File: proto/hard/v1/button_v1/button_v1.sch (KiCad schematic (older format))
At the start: 61 parts, among them J1 Conn_01x06_Female, J10 Conn_01x04_Male, J14 K3-2235D, J2 Conn_01x06_Female, J3 Conn_01x06_Female, J4 Conn_01x06_Female, J7 Conn_01x04_Female, J9 Conn_01x06_Male, Q1 TP0610T, Q3 TP0610T, Q6 UMG8N, Q7 UMG8N, Q8 IRLML2803, U1 LCD_2.8_SPI, U11 TC305, U12 LCD_1_8_SPI, U13 74HC595, U2 STM32F103C8Tx, U6 LM339, Y1 8MHz

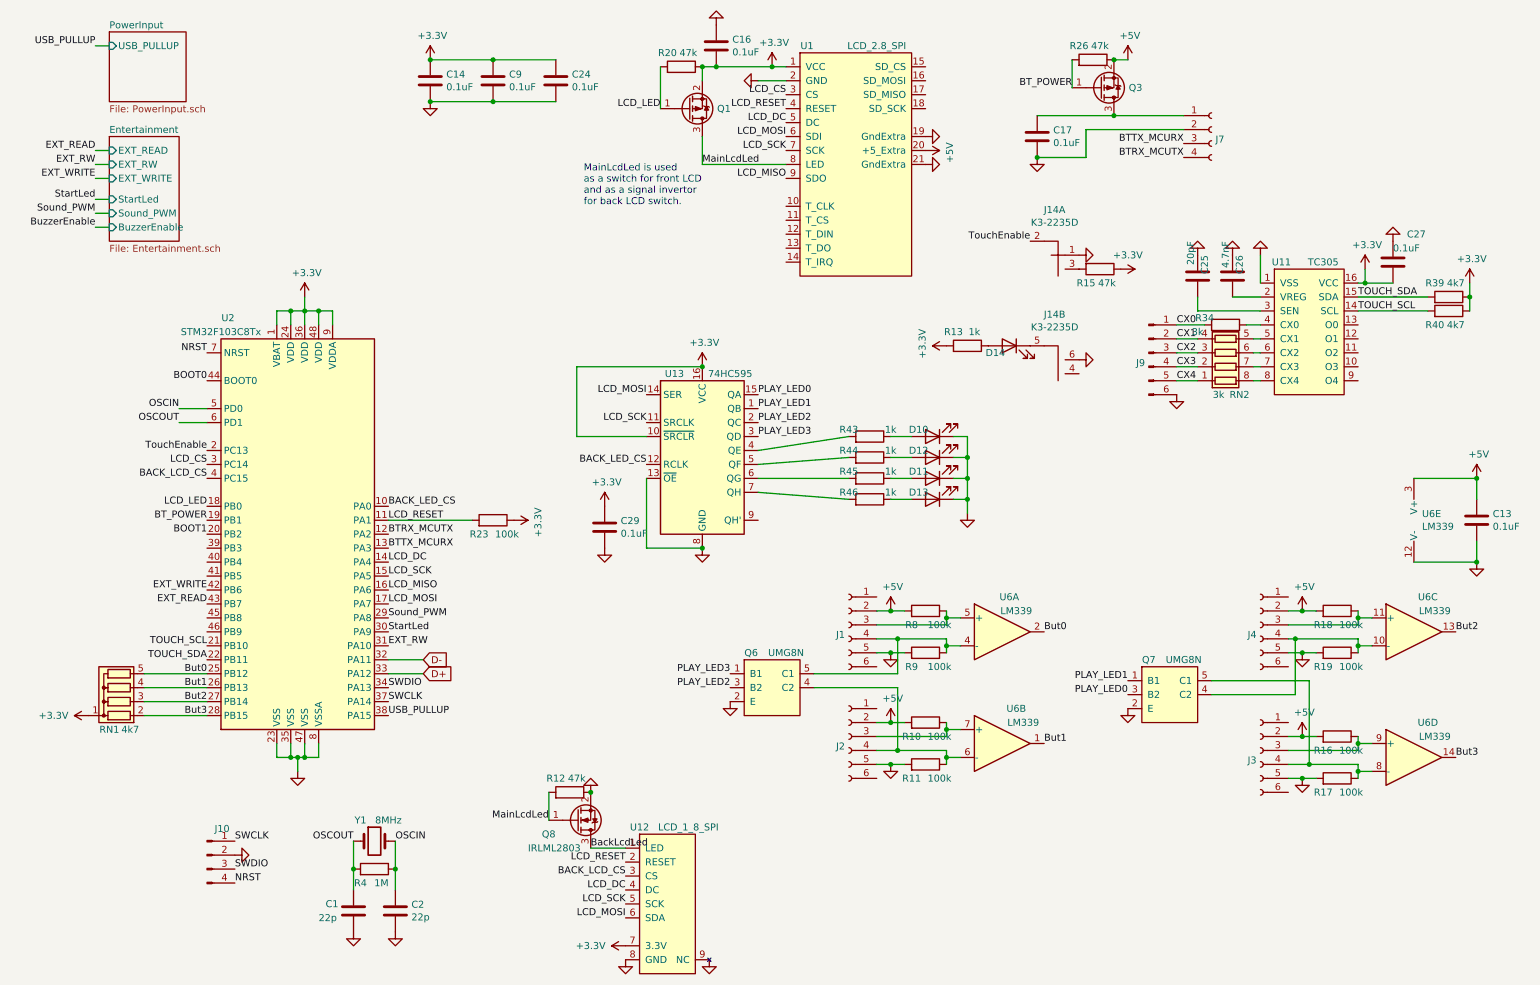
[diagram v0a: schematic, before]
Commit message: Moved buttons to separate sheet. Added replacement transistors for buttons.
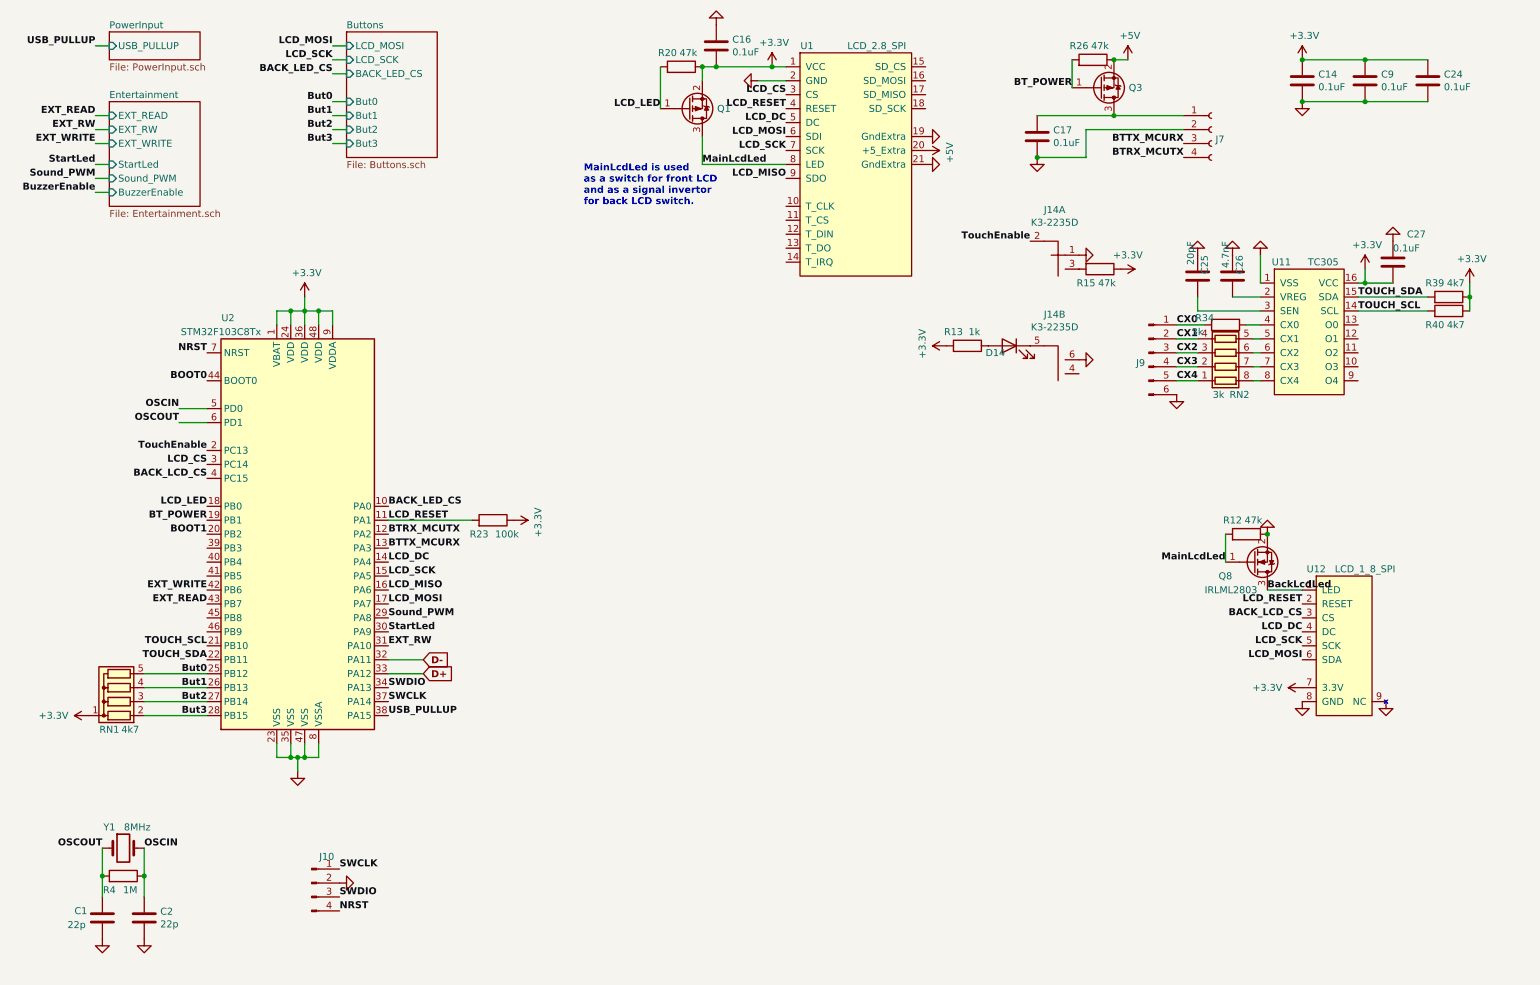
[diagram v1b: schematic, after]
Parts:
- removed C13, C29: 0.1uF, Capacitor_SMD:C_0805_2012Metric_Pad1.15x1.40mm_HandSolder, symbol Device:C
- removed D10, D11, D12, D13: LED, LED_THT:LED_D3.0mm_Clear, symbol Device:LED
- removed J1, J2, J3, J4: Conn_01x06_Female, Connector_RJ:RJ12_Amphenol_54601, symbol Connector:Conn_01x06_Female
- removed Q6, Q7: UMG8N, Package_TO_SOT_SMD:SOT-353_SC-70-5_Handsoldering, symbol brbuttonsystem:UMG8N
- removed R10, R11, R16, R17, R18, R19, R8, R9: 100k, Resistor_SMD:R_0805_2012Metric_Pad1.15x1.40mm_HandSolder, symbol Device:R
- removed R43, R44, R45, R46: 1k, Resistor_SMD:R_0805_2012Metric_Pad1.15x1.40mm_HandSolder, symbol Device:R
- removed U13: 74HC595, Package_SO:SOIC-16_3.9x9.9mm_P1.27mm, symbol 74xx:74HC595
- removed U6: LM339, Package_SO:SOIC-14_3.9x8.7mm_P1.27mm, symbol Comparator:LM339
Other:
- moved on the sheet: C1, C14, C2, C24, C9, J10, Q8, R12, R4, U12, Y1

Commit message: BOOT0 connected to GND Due to migration to Kicad V5.1.6 had to change text style from "bold" to "normal"
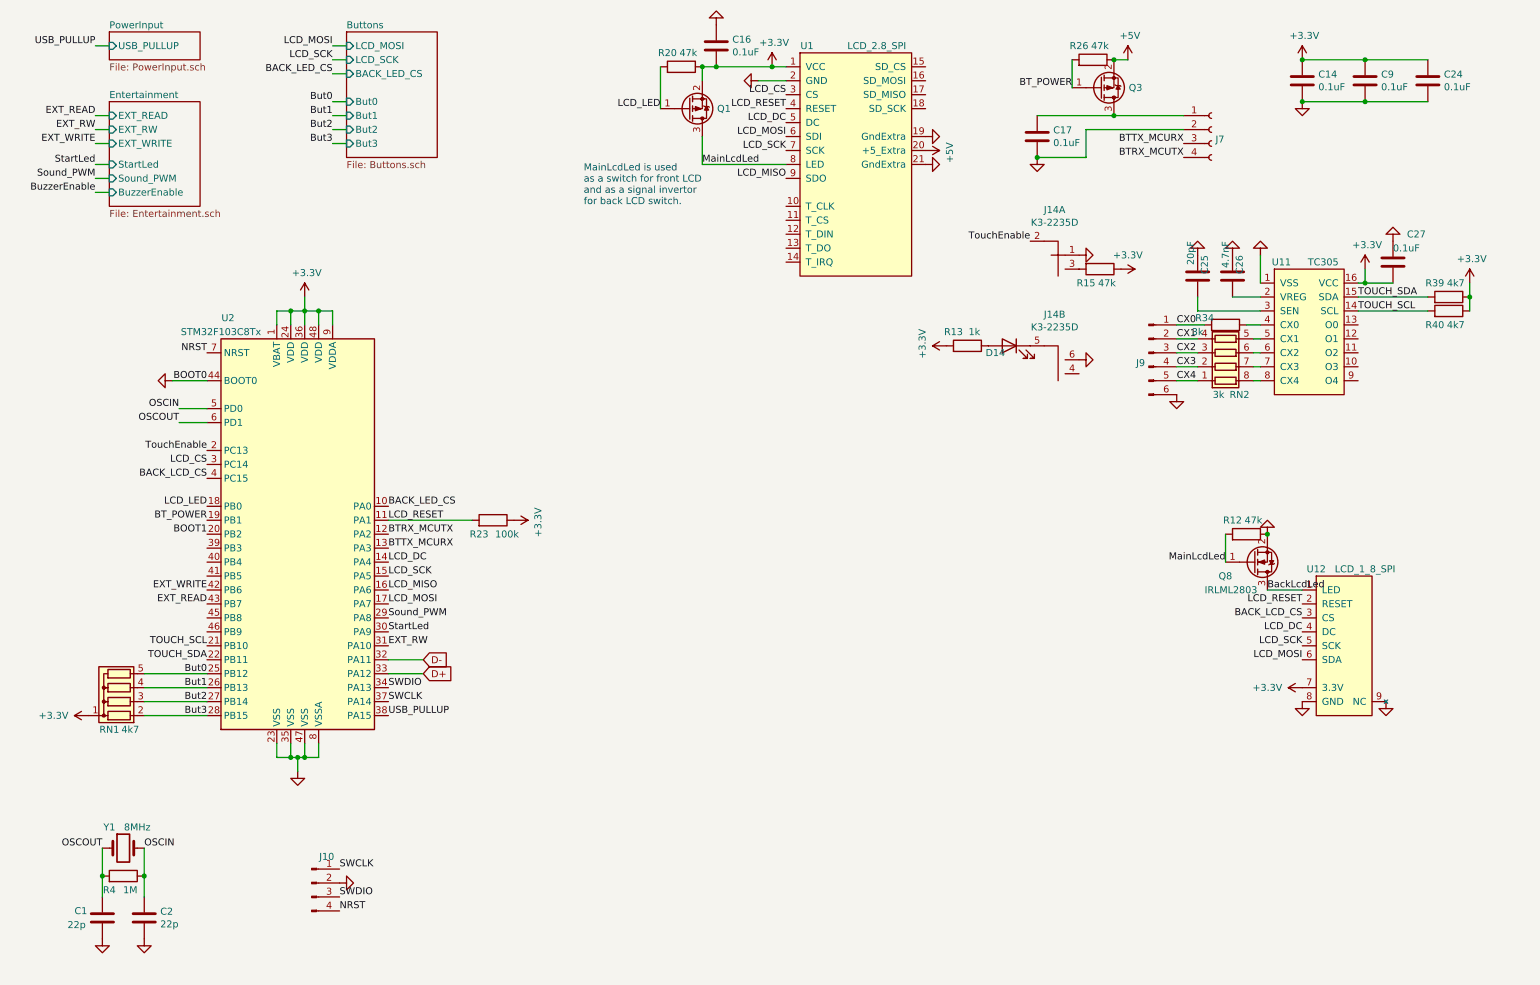
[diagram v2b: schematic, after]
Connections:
- net BOOT0 is gone; now on net GND: U2.44 (BOOT0)
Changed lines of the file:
@@
 EESchema Schematic File Version 4
-LIBS:button_v1-cache
-EELAYER 29 0
+EELAYER 30 0
 EELAYER END
 $Descr A4 11693 8268
@@
 	1    0    0    -1
 $EndComp
-Text Label 1400 6550 0    50   ~ 6
+Text Label 1400 6550 0    50   ~ 0
 OSCIN
-Text Label 1100 6550 2    50   ~ 6
+Text Label 1100 6550 2    50   ~ 0
 OSCOUT
 $Comp
@@
 Wire Wire Line
 	6000 950  5900 950
-Text Label 6000 1450 2    50   ~ 6
+Text Label 6000 1450 2    50   ~ 0
 LCD_MOSI
-Text Label 6000 1750 2    50   ~ 6
+Text Label 6000 1750 2    50   ~ 0
 LCD_MISO
-Text Label 6000 1550 2    50   ~ 6
+Text Label 6000 1550 2    50   ~ 0
 LCD_SCK
 $Comp
@@
 Wire Wire Line
 	5400 1650 6000 1650
-Text Label 5100 1250 2    50   ~ 6
+Text Label 5100 1250 2    50   ~ 0
 LCD_LED
-Text Label 6000 1250 2    50   ~ 6
+Text Label 6000 1250 2    50   ~ 0
 LCD_RESET
-Text Label 6000 1150 2    50   ~ 6
+Text Label 6000 1150 2    50   ~ 0
 LCD_CS
-Text Label 6000 1350 2    50   ~ 6
+Text Label 6000 1350 2    50   ~ 0
 LCD_DC
 $Comp
@@
 Wire Wire Line
 	3750 4200 3150 4200
-Text Label 1850 5100 2    50   ~ 6
+Text Label 1850 5100 2    50   ~ 0
 TOUCH_SCL
-Text Label 1850 5200 2    50   ~ 6
+Text Label 1850 5200 2    50   ~ 0
 TOUCH_SDA
-Text Label 3150 4900 0    50   ~ 6
+Text Label 3150 4900 0    50   ~ 0
 Sound_PWM
-Text Label 1850 4200 2    50   ~ 6
+Text Label 1850 4200 2    50   ~ 0
 BT_POWER
-Text Label 3150 4400 0    50   ~ 6
+Text Label 3150 4400 0    50   ~ 0
 BTTX_MCURX
-Text Label 3150 4300 0    50   ~ 6
+Text Label 3150 4300 0    50   ~ 0
 BTRX_MCUTX
-Text Label 3150 5000 0    50   ~ 6
+Text Label 3150 5000 0    50   ~ 0
 StartLed
-Text Label 3150 5100 0    50   ~ 6
+Text Label 3150 5100 0    50   ~ 0
 EXT_RW
-Text Label 1850 4800 2    50   ~ 6
+Text Label 1850 4800 2    50   ~ 0
 EXT_READ
-Text Label 1850 4700 2    50   ~ 6
+Text Label 1850 4700 2    50   ~ 0
 EXT_WRITE
 $Comp
@@
 	0    1    -1   0
 $EndComp
-Text Label 1850 3800 2    50   ~ 6
+Text Label 1850 3800 2    50   ~ 0
 LCD_CS
-Text Label 3150 4200 0    50   ~ 6
+Text Label 3150 4200 0    50   ~ 0
 LCD_RESET
-Text Label 3150 4500 0    50   ~ 6
+Text Label 3150 4500 0    50   ~ 0
 LCD_DC
-Text Label 1850 4100 2    50   ~ 6
+Text Label 1850 4100 2    50   ~ 0
 LCD_LED
-Text Label 3150 4600 0    50   ~ 6
+Text Label 3150 4600 0    50   ~ 0
 LCD_SCK
-Text Label 3150 4700 0    50   ~ 6
+Text Label 3150 4700 0    50   ~ 0
 LCD_MISO
 $Comp
@@
 	1    0    0    -1
 $EndComp
-Text Label 3150 4800 0    50   ~ 6
+Text Label 3150 4800 0    50   ~ 0
 LCD_MOSI
 $Comp
@@
 	0    -1   -1   0
 $EndComp
-Text Label 1850 5600 2    50   ~ 6
+Text Label 1850 5600 2    50   ~ 0
 But3
-Text Label 1850 5500 2    50   ~ 6
+Text Label 1850 5500 2    50   ~ 0
 But2
-Text Label 1850 5400 2    50   ~ 6
+Text Label 1850 5400 2    50   ~ 0
 But1
-Text Label 1850 5300 2    50   ~ 6
+Text Label 1850 5300 2    50   ~ 0
 But0
 Wire Wire Line
@@
 Wire Wire Line
 	1650 3400 1850 3400
-Text Label 1650 3400 2    50   ~ 6
+Text Label 1650 3400 2    50   ~ 0
 OSCIN
-Text Label 1650 3500 2    50   ~ 6
+Text Label 1650 3500 2    50   ~ 0
 OSCOUT
 Wire Wire Line
@@
 	1    0    0    -1
 $EndComp
-Text Label 3150 5400 0    50   ~ 6
+Text Label 3150 5400 0    50   ~ 0
 SWDIO
-Text Label 3150 5500 0    50   ~ 6
+Text Label 3150 5500 0    50   ~ 0
 SWCLK
-Text Label 1850 3000 2    50   ~ 6
-NRST
-Text Label 1850 3200 2    50   ~ 6
+Text Label 1850 3200 2    50   ~ 0
 BOOT0
-Text Label 1850 4300 2    50   ~ 6
+Text Label 1850 4300 2    50   ~ 0
 BOOT1
-Text Label 1850 3700 2    50   ~ 6
+Text Label 1850 3700 2    50   ~ 0
 TouchEnable
 $Comp
@@
 Wire Wire Line
 	8050 900  8050 1100
-Text Label 8050 1100 2    50   ~ 6
+Text Label 8050 1100 2    50   ~ 0
 BT_POWER
 $Comp
@@
 	0    -1   -1   0
 $EndComp
-Text Label 7750 2200 2    50   ~ 6
+Text Label 7750 2200 2    50   ~ 0
 TouchEnable
 $Comp
@@
 	0    -1   -1   0
 $EndComp
-Text Label 8800 3200 0    50   ~ 6
+Text Label 8800 3200 0    50   ~ 0
 CX4
-Text Label 8800 3100 0    50   ~ 6
+Text Label 8800 3100 0    50   ~ 0
 CX3
-Text Label 8800 3000 0    50   ~ 6
+Text Label 8800 3000 0    50   ~ 0
 CX2
-Text Label 8800 2900 0    50   ~ 6
+Text Label 8800 2900 0    50   ~ 0
 CX1
-Text Label 8800 2800 0    50   ~ 6
+Text Label 8800 2800 0    50   ~ 0
 CX0
 Wire Wire Line
@@
 	0    1    -1   0
 $EndComp
-Text Label 10100 2600 0    50   ~ 6
+Text Label 10100 2600 0    50   ~ 0
 TOUCH_SDA
 Wire Wire Line
 	10150 2500 10350 2500
-Text Label 10100 2700 0    50   ~ 6
+Text Label 10100 2700 0    50   ~ 0
 TOUCH_SCL
 Connection ~ 10150 2500
@@
 F7 "BuzzerEnable" I L 1150 1850 50
 $EndSheet
-Text Label 1050 1300 2    50   ~ 6
+Text Label 1050 1300 2    50   ~ 0
 EXT_READ
-Text Label 1050 1400 2    50   ~ 6
+Text Label 1050 1400 2    50   ~ 0
 EXT_RW
-Text Label 1050 1500 2    50   ~ 6
+Text Label 1050 1500 2    50   ~ 0
 EXT_WRITE
-Text Label 1050 1650 2    50   ~ 6
+Text Label 1050 1650 2    50   ~ 0
 StartLed
-Text Label 1050 1750 2    50   ~ 6
+Text Label 1050 1750 2    50   ~ 0
 Sound_PWM
 Wire Wire Line
@@
 Wire Wire Line
 	1150 1300 1050 1300
-Text GLabel 3400 5300 2    50   Input ~ 6
+Text GLabel 3400 5300 2    50   Input ~ 0
 D+
-Text GLabel 3400 5200 2    50   Input ~ 6
+Text GLabel 3400 5200 2    50   Input ~ 0
 D-
 $Sheet
@@
 Connection ~ 9700 900
 Connection ~ 9700 1200
-Text Label 3150 4100 0    50   ~ 6
+Text Label 3150 4100 0    50   ~ 0
 BACK_LED_CS
-Text Label 1050 1850 2    50   ~ 6
+Text Label 1050 1850 2    50   ~ 0
 BuzzerEnable
 Wire Wire Line
 	1050 1850 1150 1850
-Text Label 2800 7000 0    50   ~ 6
+Text Label 2800 7000 0    50   ~ 0
 NRST
-Text Label 2800 6700 0    50   ~ 6
+Text Label 2800 6700 0    50   ~ 0
 SWCLK
-Text Label 2800 6900 0    50   ~ 6
+Text Label 2800 6900 0    50   ~ 0
 SWDIO
 $Comp
@@
 	1    0    0    -1
 $EndComp
-Text Label 9700 5100 2    50   ~ 6
+Text Label 9700 5100 2    50   ~ 0
 LCD_SCK
-Text Label 9700 5200 2    50   ~ 6
+Text Label 9700 5200 2    50   ~ 0
 LCD_MOSI
-Text Label 9700 5000 2    50   ~ 6
+Text Label 9700 5000 2    50   ~ 0
 LCD_DC
 $Comp
@@
 $EndComp
 Connection ~ 9450 4300
-Text Label 5400 1650 0    50   ~ 6
+Text Label 5400 1650 0    50   ~ 0
 MainLcdLed
-Text Label 9450 4700 0    50   ~ 6
+Text Label 9450 4700 0    50   ~ 0
 BackLcdLed
-Text Label 8850 1600 2    50   ~ 6
+Text Label 8850 1600 2    50   ~ 0
 BTRX_MCUTX
-Text Label 8850 1500 2    50   ~ 6
+Text Label 8850 1500 2    50   ~ 0
 BTTX_MCURX
 $Comp
@@
 	0    -1   -1   0
 $EndComp
-Text Label 9700 4900 2    50   ~ 6
+Text Label 9700 4900 2    50   ~ 0
 BACK_LCD_CS
 $Comp
@@
 	1    0    0    -1
 $EndComp
-Text Label 9700 4800 2    50   ~ 6
+Text Label 9700 4800 2    50   ~ 0
 LCD_RESET
 $Comp
@@
 	1    0    0    -1
 $EndComp
-Text Label 1850 3900 2    50   ~ 6
+Text Label 1850 3900 2    50   ~ 0
 BACK_LCD_CS
-Text Label 9150 4500 2    50   ~ 6
-MainLcdLed
-Text Notes 4550 1950 0    50   ~ 6
+Text Notes 4550 1950 0    50   ~ 0
 MainLcdLed is used\nas a switch for front LCD\nand as a signal invertor\nfor back LCD switch.
-Text Label 3150 5600 0    50   ~ 6
+Text Label 3150 5600 0    50   ~ 0
 USB_PULLUP
 $Comp
@@
 Wire Wire Line
 	8800 3200 8950 3200
-Text Label 1050 800  2    50   ~ 6
+Text Label 1050 800  2    50   ~ 0
 USB_PULLUP
 Wire Wire Line
@@
 F8 "But3" I L 2850 1500 50
 $EndSheet
-Text Label 2750 800  2    50   ~ 6
+Text Label 2750 800  2    50   ~ 0
 LCD_MOSI
-Text Label 2750 900  2    50   ~ 6
+Text Label 2750 900  2    50   ~ 0
 LCD_SCK
-Text Label 2750 1000 2    50   ~ 6
+Text Label 2750 1000 2    50   ~ 0
 BACK_LED_CS
 Wire Wire Line
@@
 Wire Wire Line
 	2750 800  2850 800
-Text Label 2750 1200 2    50   ~ 6
+Text Label 2750 1200 2    50   ~ 0
 But0
-Text Label 2750 1300 2    50   ~ 6
+Text Label 2750 1300 2    50   ~ 0
 But1
-Text Label 2750 1400 2    50   ~ 6
+Text Label 2750 1400 2    50   ~ 0
 But2
-Text Label 2750 1500 2    50   ~ 6
+Text Label 2750 1500 2    50   ~ 0
 But3
 Wire Wire Line
@@
 Wire Wire Line
 	2850 1500 2750 1500
+$Comp
+L power:GND #PWR0168
+U 1 1 5F134F3D
+P 1600 3200
+F 0 "#PWR0168" H 1600 2950 50  0001 C CNN
+F 1 "GND" H 1605 3027 50  0001 C CNN
+F 2 "" H 1600 3200 50  0001 C CNN
+F 3 "" H 1600 3200 50  0001 C CNN
+	1    1600 3200
+	0    1    1    0
+$EndComp
+Wire Wire Line
+	1600 3200 1850 3200
+Text Label 1850 3000 2    50   ~ 0
+NRST
+Text Label 9150 4500 2    50   ~ 0
+MainLcdLed
 $EndSCHEMATC
